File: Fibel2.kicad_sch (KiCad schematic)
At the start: 0 parts

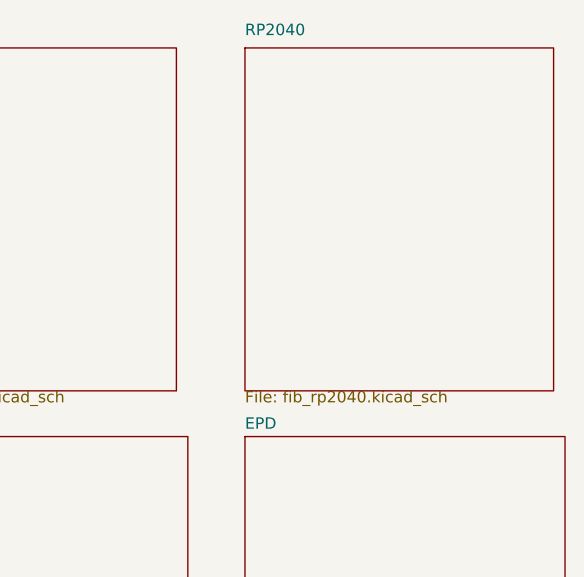
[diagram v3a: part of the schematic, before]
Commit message: restructured EPD side of things, replaced rp2040 with esp32 s3 because of it's LCD controller, USB, LP WIFI_BT & EPDiy compat, repurposed USB0 for ESP interfacing, added e-ink pmic
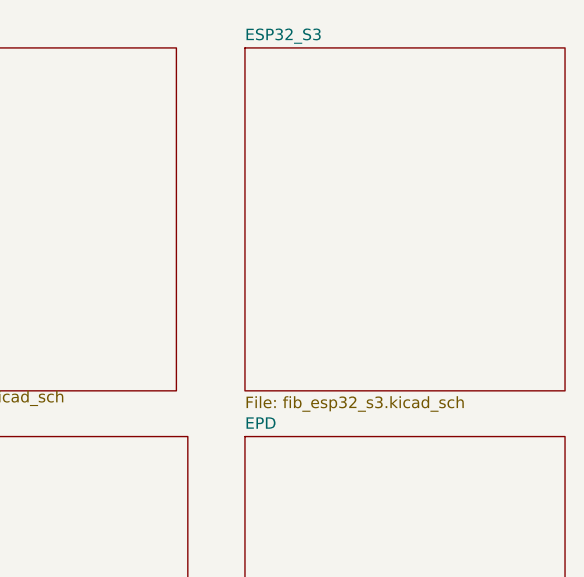
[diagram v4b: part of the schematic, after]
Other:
- removed sheet RP2040
- added sheet ESP32_S3 (fib_esp32_s3.kicad_sch)
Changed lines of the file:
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@@
-	)
-	(sheet
-		(at 196.85 20.32)
-		(size 34.29 38.1)
-		(fields_autoplaced yes)
-		(stroke
-			(width 0.1524)
-			(type solid)
-		)
-		(fill
-			(color 0 0 0 0.0000)
-		)
-		(property "Sheetname" "RP2040"
-			(at 196.85 19.05 0)
-			(effects
-				(font
-					(size 1.27 1.27)
-				)
-				(justify left bottom)
-			)
-		)
-		(property "Sheetfile" "fib_rp2040.kicad_sch"
-			(at 196.85 58.3696 0)
-			(effects
-				(font
-					(size 1.27 1.27)
-				)
-				(justify left top)
-			)
-		)
-		(instances
-			(project "Fibel2"
-				(path "/862c21e2-7ec9-4f80-a33c-aad02ea9423e"
-					(page "5")
-				)
-			)
-		)
 	)
 	(sheet
@@
 				)
 			)
+		)
+	)
+	(sheet
+		(at 196.85 20.32)
+		(size 35.56 38.1)
+		(fields_autoplaced yes)
+		(stroke
+			(width 0.1524)
+			(type solid)
+		)
+		(fill
+			(color 0 0 0 0.0000)
+		)
+		(property "Sheetname" "ESP32_S3"
+			(at 196.85 19.6084 0)
+			(effects
+				(font
+					(size 1.27 1.27)
+				)
+				(justify left bottom)
+			)
+		)
+		(property "Sheetfile" "fib_esp32_s3.kicad_sch"
+			(at 196.85 59.0046 0)
+			(effects
+				(font
+					(size 1.27 1.27)
+				)
+				(justify left top)
+			)
+		)
+		(instances
+			(project "Fibel2"
+				(path "/862c21e2-7ec9-4f80-a33c-aad02ea9423e"
+					(page "12")
+				)
+			)

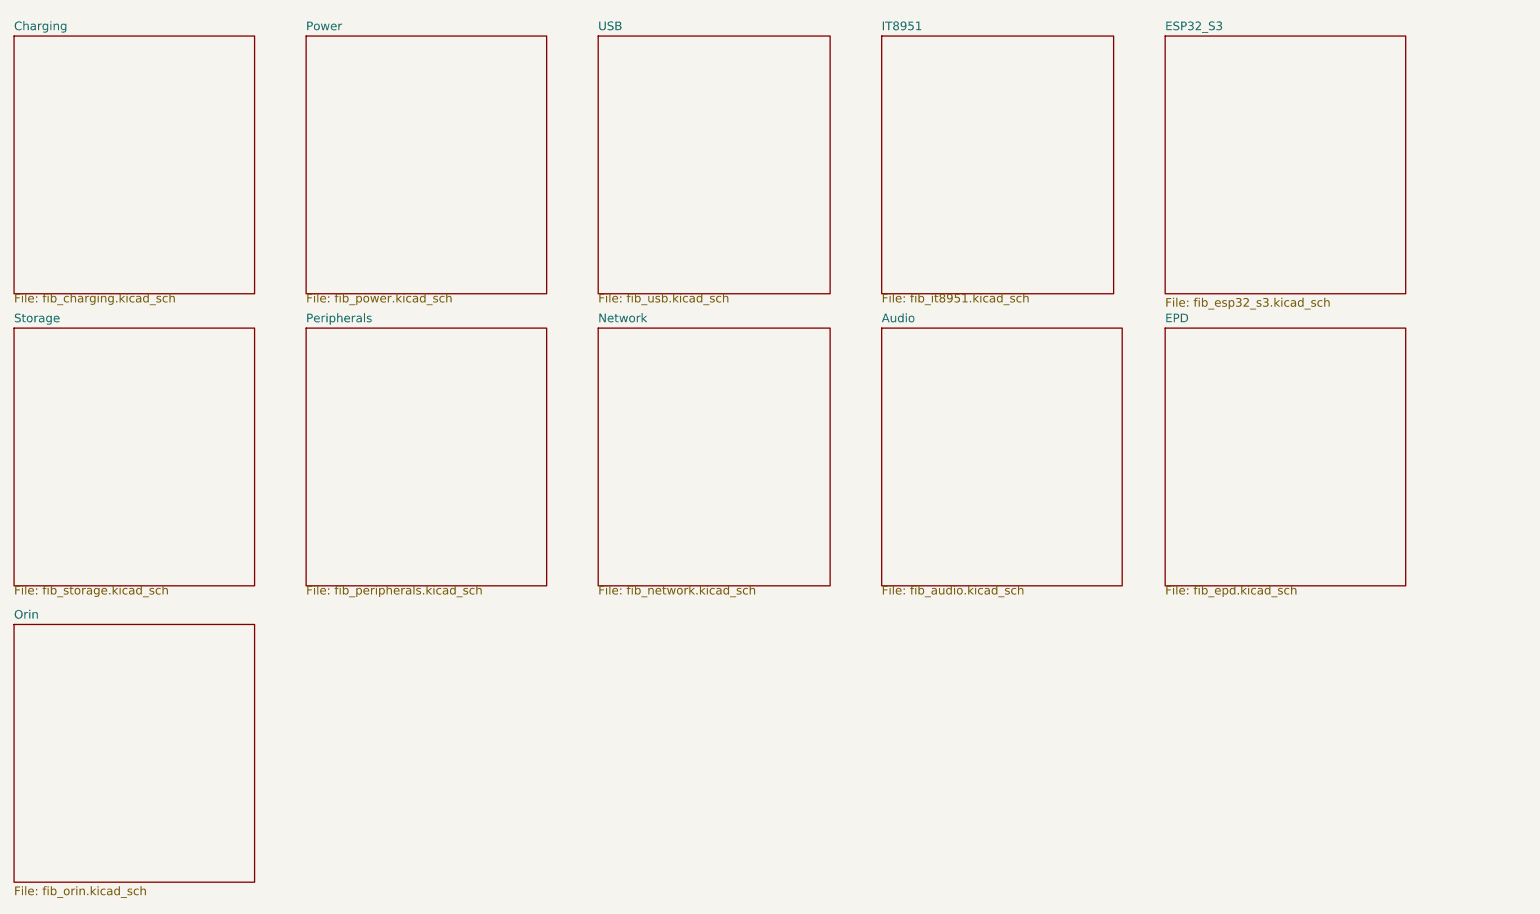
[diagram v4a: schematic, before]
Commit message: added buck converter, refactoored peripherals and updated gpio/SPI/i2c mapping
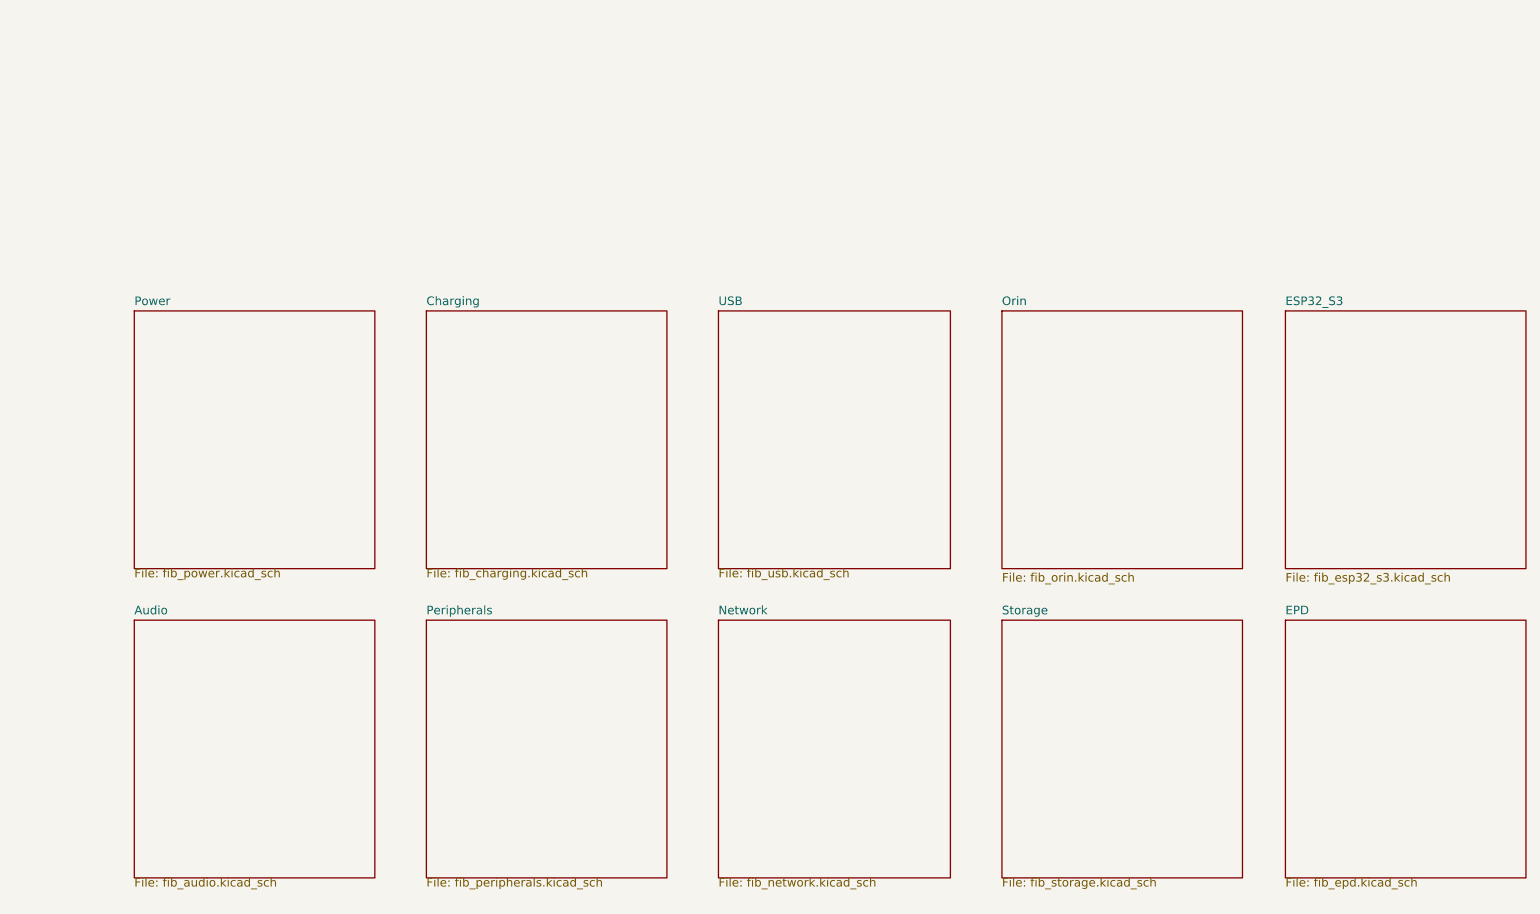
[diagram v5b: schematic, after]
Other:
- removed sheet IT8951
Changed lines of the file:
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@@
 	(paper "A4")
 	(sheet
-		(at 154.94 63.5)
+		(at 44.45 106.68)
 		(size 35.56 38.1)
 		(fields_autoplaced yes)
@@
 		)
 		(property "Sheetname" "Audio"
-			(at 154.94 62.7884 0)
+			(at 44.45 105.9684 0)
 			(effects
 				(font
@@
 		)
 		(property "Sheetfile" "fib_audio.kicad_sch"
-			(at 154.94 101.5496 0)
+			(at 44.45 144.7296 0)
 			(effects
 				(font
@@
 	)
 	(sheet
-		(at 26.67 20.32)
+		(at 87.63 60.96)
 		(size 35.56 38.1)
 		(fields_autoplaced yes)
@@
 		)
 		(property "Sheetname" "Charging"
-			(at 26.67 19.6084 0)
+			(at 87.63 60.2484 0)
 			(effects
 				(font
@@
 		)
 		(property "Sheetfile" "fib_charging.kicad_sch"
-			(at 26.67 58.3696 0)
+			(at 87.63 99.0096 0)
 			(effects
 				(font
@@
 	)
 	(sheet
-		(at 26.67 107.315)
+		(at 172.72 60.96)
 		(size 35.56 38.1)
 		(fields_autoplaced yes)
@@
 		)
 		(property "Sheetname" "Orin"
-			(at 26.67 106.6034 0)
+			(at 172.72 60.2484 0)
 			(effects
 				(font
@@
 		)
 		(property "Sheetfile" "fib_orin.kicad_sch"
-			(at 26.67 145.9996 0)
-			(effects
-				(font
-					(size 1.27 1.27)
-				)
-				(justify left top)
-			)
-		)
-		(instances
-			(project "Fibel2"
-				(path "/862c21e2-7ec9-4f80-a33c-aad02ea9423e"
-					(page "11")
-				)
-			)
-		)
-	)
-	(sheet
-		(at 196.85 20.32)
+			(at 172.72 99.6446 0)
+			(effects
+				(font
+					(size 1.27 1.27)
+				)
+				(justify left top)
+			)
+		)
+		(instances
+			(project "Fibel2"
+				(path "/862c21e2-7ec9-4f80-a33c-aad02ea9423e"
+					(page "4")
+				)
+			)
+		)
+	)
+	(sheet
+		(at 214.63 60.96)
 		(size 35.56 38.1)
 		(fields_autoplaced yes)
@@
 		)
 		(property "Sheetname" "ESP32_S3"
-			(at 196.85 19.6084 0)
+			(at 214.63 60.2484 0)
 			(effects
 				(font
@@
 		)
 		(property "Sheetfile" "fib_esp32_s3.kicad_sch"
-			(at 196.85 59.0046 0)
-			(effects
-				(font
-					(size 1.27 1.27)
-				)
-				(justify left top)
-			)
-		)
-		(instances
-			(project "Fibel2"
-				(path "/862c21e2-7ec9-4f80-a33c-aad02ea9423e"
-					(page "12")
-				)
-			)
-		)
-	)
-	(sheet
-		(at 196.85 63.5)
+			(at 214.63 99.6446 0)
+			(effects
+				(font
+					(size 1.27 1.27)
+				)
+				(justify left top)
+			)
+		)
+		(instances
+			(project "Fibel2"
+				(path "/862c21e2-7ec9-4f80-a33c-aad02ea9423e"
+					(page "5")
+				)
+			)
+		)
+	)
+	(sheet
+		(at 214.63 106.68)
 		(size 35.56 38.1)
 		(fields_autoplaced yes)
@@
 		)
 		(property "Sheetname" "EPD"
-			(at 196.85 62.7884 0)
+			(at 214.63 105.9684 0)
 			(effects
 				(font
@@
 		)
 		(property "Sheetfile" "fib_epd.kicad_sch"
-			(at 196.85 101.5496 0)
+			(at 214.63 144.7296 0)
 			(effects
 				(font
@@
 	)
 	(sheet
-		(at 26.67 63.5)
+		(at 172.72 106.68)
 		(size 35.56 38.1)
 		(fields_autoplaced yes)
@@
 		)
 		(property "Sheetname" "Storage"
-			(at 26.67 62.7884 0)
+			(at 172.72 105.9684 0)
 			(effects
 				(font
@@
 		)
 		(property "Sheetfile" "fib_storage.kicad_sch"
-			(at 26.67 101.5496 0)
+			(at 172.72 144.7296 0)
 			(effects
 				(font
@@
 	)
 	(sheet
-		(at 69.85 20.32)
+		(at 44.45 60.96)
 		(size 35.56 38.1)
 		(fields_autoplaced yes)
@@
 		)
 		(property "Sheetname" "Power"
-			(at 69.85 19.6084 0)
+			(at 44.45 60.2484 0)
 			(effects
 				(font
@@
 		)
 		(property "Sheetfile" "fib_power.kicad_sch"
-			(at 69.85 58.3696 0)
+			(at 44.45 99.0096 0)
 			(effects
 				(font
@@
 	)
 	(sheet
-		(at 113.03 20.32)
+		(at 130.81 60.96)
 		(size 34.29 38.1)
 		(fields_autoplaced yes)
@@
 		)
 		(property "Sheetname" "USB"
-			(at 113.03 19.6084 0)
+			(at 130.81 60.2484 0)
 			(effects
 				(font
@@
 		)
 		(property "Sheetfile" "fib_usb.kicad_sch"
-			(at 113.03 58.3696 0)
+			(at 130.81 99.0096 0)
 			(effects
 				(font
@@
 	)
 	(sheet
-		(at 69.85 63.5)
+		(at 87.63 106.68)
 		(size 35.56 38.1)
 		(fields_autoplaced yes)
@@
 		)
 		(property "Sheetname" "Peripherals"
-			(at 69.85 62.7884 0)
+			(at 87.63 105.9684 0)
 			(effects
 				(font
@@
 		)
 		(property "Sheetfile" "fib_peripherals.kicad_sch"
-			(at 69.85 101.5496 0)
+			(at 87.63 144.7296 0)
 			(effects
 				(font
@@
 	)
 	(sheet
-		(at 113.03 63.5)
+		(at 130.81 106.68)
 		(size 34.29 38.1)
 		(fields_autoplaced yes)
@@
 		)
 		(property "Sheetname" "Network"
-			(at 113.03 62.7884 0)
+			(at 130.81 105.9684 0)
 			(effects
 				(font
@@
 		)
 		(property "Sheetfile" "fib_network.kicad_sch"
-			(at 113.03 101.5496 0)
+			(at 130.81 144.7296 0)
 			(effects
 				(font
@@
 				)
 			)
-		)
-	)
-	(sheet
-		(at 154.94 20.32)
-		(size 34.29 38.1)
-		(fields_autoplaced yes)
-		(stroke
-			(width 0.1524)
-			(type solid)
-		)
-		(fill
-			(color 0 0 0 0.0000)
-		)
-		(property "Sheetname" "IT8951"
-			(at 154.94 19.6084 0)
-			(effects
-				(font
-					(size 1.27 1.27)
-				)
-				(justify left bottom)
-			)
-		)
-		(property "Sheetfile" "fib_it8951.kicad_sch"
-			(at 154.94 58.3696 0)
-			(effects
-				(font
-					(size 1.27 1.27)
-				)
-				(justify left top)
-			)
-		)
-		(instances
-			(project "Fibel2"
-				(path "/862c21e2-7ec9-4f80-a33c-aad02ea9423e"
-					(page "4")
-				)
-			)

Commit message: added connections to ESP32 S3, most oof EPD stuff that we're gooing to use is included
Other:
- removed sheet ESP32_S3
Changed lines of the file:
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@@
 			(color 0 0 0 0.0000)
 		)
-		(property "Sheetname" "ESP32_S3"
+		(property "Sheetname" "EPD"
 			(at 214.63 60.2484 0)
 			(effects
@@
 			)
 		)
-		(property "Sheetfile" "fib_esp32_s3.kicad_sch"
-			(at 214.63 99.6446 0)
+		(property "Sheetfile" "fib_epd.kicad_sch"
+			(at 214.63 99.0096 0)
 			(effects
 				(font
@@
 				)
 			)
-		)
-	)
-	(sheet
-		(at 214.63 106.68)
-		(size 35.56 38.1)
-		(fields_autoplaced yes)
-		(stroke
-			(width 0.1524)
-			(type solid)
-		)
-		(fill
-			(color 0 0 0 0.0000)
-		)
-		(property "Sheetname" "EPD"
-			(at 214.63 105.9684 0)
-			(effects
-				(font
-					(size 1.27 1.27)
-				)
-				(justify left bottom)
-			)
-		)
-		(property "Sheetfile" "fib_epd.kicad_sch"
-			(at 214.63 144.7296 0)
-			(effects
-				(font
-					(size 1.27 1.27)
-				)
-				(justify left top)
-			)
-		)
-		(instances
-			(project "Fibel2"
-				(path "/862c21e2-7ec9-4f80-a33c-aad02ea9423e"
-					(page "10")
-				)
-			)

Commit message: refactored PCIe pages
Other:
- sheet Network renamed PCIe
- removed sheet Storage
- sheet PCIe: file fib_network.kicad_sch -> fib_pcie.kicad_sch
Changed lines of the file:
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@@
-	)
-	(sheet
-		(at 172.72 106.68)
-		(size 35.56 38.1)
-		(fields_autoplaced yes)
-		(stroke
-			(width 0.1524)
-			(type solid)
-		)
-		(fill
-			(color 0 0 0 0.0000)
-		)
-		(property "Sheetname" "Storage"
-			(at 172.72 105.9684 0)
-			(effects
-				(font
-					(size 1.27 1.27)
-				)
-				(justify left bottom)
-			)
-		)
-		(property "Sheetfile" "fib_storage.kicad_sch"
-			(at 172.72 144.7296 0)
-			(effects
-				(font
-					(size 1.27 1.27)
-				)
-				(justify left top)
-			)
-		)
-		(instances
-			(project "Fibel2"
-				(path "/862c21e2-7ec9-4f80-a33c-aad02ea9423e"
-					(page "9")
-				)
-			)
-		)
 	)
 	(sheet
@@
 			(color 0 0 0 0.0000)
 		)
-		(property "Sheetname" "Network"
+		(property "Sheetname" "PCIe"
 			(at 130.81 105.9684 0)
 			(effects
@@
 			)
 		)
-		(property "Sheetfile" "fib_network.kicad_sch"
+		(property "Sheetfile" "fib_pcie.kicad_sch"
 			(at 130.81 144.7296 0)
 			(effects
